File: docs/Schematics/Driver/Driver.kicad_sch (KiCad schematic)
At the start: 7 parts, among them J10 AUX_3V3, J11 AUX_GND, J9 AUX_5V

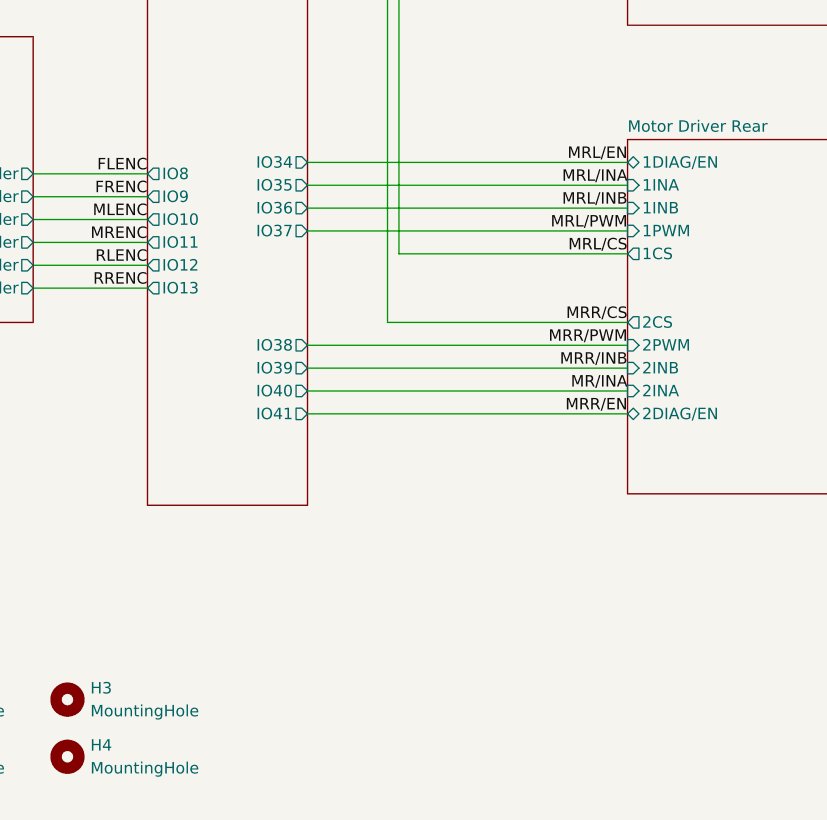
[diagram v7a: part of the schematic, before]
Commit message: First version of the routed board is done
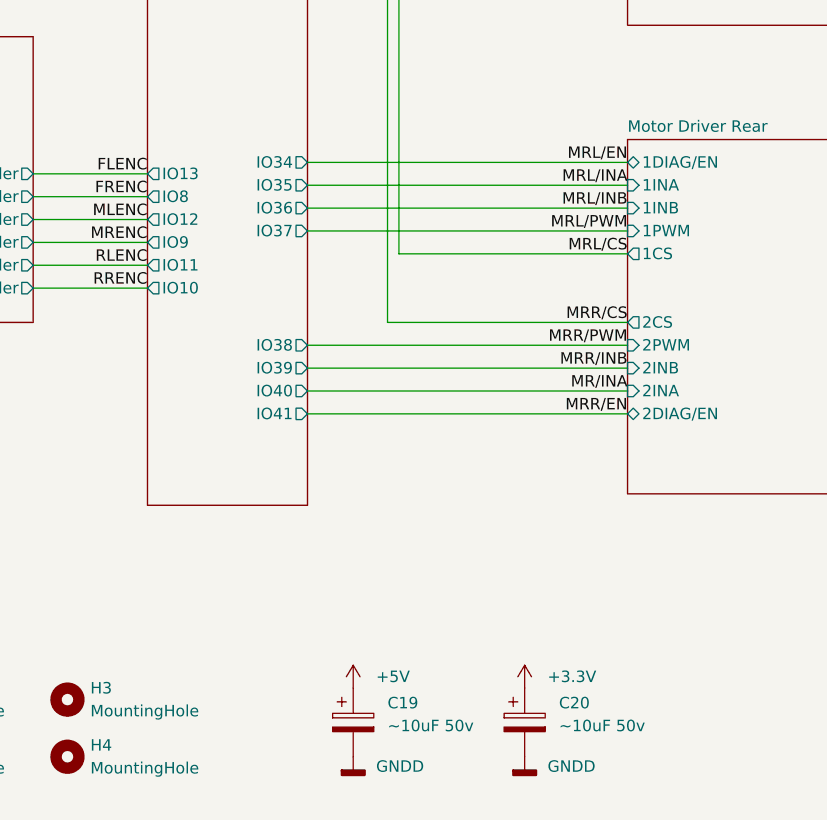
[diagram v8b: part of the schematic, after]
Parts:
- added C19, C20: ~10uF 50v, Capacitor_THT:CP_Radial_D8.0mm_P5.00mm, symbol Device:C_Polarized
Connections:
- net +3.3V: now also C20.1
- net +5V: now also C19.1
- net GNDD: now also C19.2, C20.2
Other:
- title: Arty Z7 IO expander card -> Arty Z7 IO Board
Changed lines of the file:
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@@
   (paper "A4")
   (title_block
-    (title "Arty Z7 IO expander card")
+    (title "Arty Z7 IO Board")
     (date "2022-12-24")
-    (rev "0.1")
+    (rev "${VER}")
     (company "HiQ")
   )
@@
     )
   )
+  (symbol (lib_id "power:GNDD") (at 127 190.5 0) (unit 1)
+    (in_bom yes) (on_board yes) (fields_autoplaced)
+    (property "Reference" "#PWR0103" (id 0) (at 127 196.85 0)
+      (effects (font (size 1.27 1.27)) hide)
+    )
+    (property "Value" "GNDD" (id 1) (at 129.54 191.5794 0)
+      (effects (font (size 1.27 1.27)) (justify left))
+    )
+    (property "Footprint" "" (id 2) (at 127 190.5 0)
+      (effects (font (size 1.27 1.27)) hide)
+    )
+    (property "Datasheet" "" (id 3) (at 127 190.5 0)
+      (effects (font (size 1.27 1.27)) hide)
+    )
+    (pin "1")
+  )
+  (symbol (lib_id "power:+5V") (at 127 182.88 0) (unit 1)
+    (in_bom yes) (on_board yes) (fields_autoplaced)
+    (property "Reference" "#PWR0105" (id 0) (at 127 186.69 0)
+      (effects (font (size 1.27 1.27)) hide)
+    )
+    (property "Value" "+5V" (id 1) (at 129.54 181.6099 0)
+      (effects (font (size 1.27 1.27)) (justify left))
+    )
+    (property "Footprint" "" (id 2) (at 127 182.88 0)
+      (effects (font (size 1.27 1.27)) hide)
+    )
+    (property "Datasheet" "" (id 3) (at 127 182.88 0)
+      (effects (font (size 1.27 1.27)) hide)
+    )
+    (pin "1")
+  )
+  (symbol (lib_id "power:GNDD") (at 146.05 190.5 0) (unit 1)
+    (in_bom yes) (on_board yes) (fields_autoplaced)
+    (property "Reference" "#PWR0104" (id 0) (at 146.05 196.85 0)
+      (effects (font (size 1.27 1.27)) hide)
+    )
+    (property "Value" "GNDD" (id 1) (at 148.59 191.5794 0)
+      (effects (font (size 1.27 1.27)) (justify left))
+    )
+    (property "Footprint" "" (id 2) (at 146.05 190.5 0)
+      (effects (font (size 1.27 1.27)) hide)
+    )
+    (property "Datasheet" "" (id 3) (at 146.05 190.5 0)
+      (effects (font (size 1.27 1.27)) hide)
+    )
+    (pin "1")
+  )
   (symbol (lib_id "Mechanical:MountingHole") (at 95.25 190.5 0) (unit 1)
     (in_bom yes) (on_board yes) (fields_autoplaced)
@@
     )
     (property "Datasheet" "" (id 3) (at 27.94 179.07 0)
+      (effects (font (size 1.27 1.27)) hide)
+    )
+    (pin "1")
+  )
+  (symbol (lib_id "Device:C_Polarized") (at 146.05 186.69 0) (unit 1)
+    (in_bom yes) (on_board yes) (fields_autoplaced)
+    (property "Reference" "C20" (id 0) (at 149.86 184.5309 0)
+      (effects (font (size 1.27 1.27)) (justify left))
+    )
+    (property "Value" "~10uF 50v" (id 1) (at 149.86 187.0709 0)
+      (effects (font (size 1.27 1.27)) (justify left))
+    )
+    (property "Footprint" "Capacitor_THT:CP_Radial_D8.0mm_P5.00mm" (id 2) (at 147.0152 190.5 0)
+      (effects (font (size 1.27 1.27)) hide)
+    )
+    (property "Datasheet" "~" (id 3) (at 146.05 186.69 0)
+      (effects (font (size 1.27 1.27)) hide)
+    )
+    (pin "1")
+    (pin "2")
+  )
+  (symbol (lib_id "Device:C_Polarized") (at 127 186.69 0) (unit 1)
+    (in_bom yes) (on_board yes) (fields_autoplaced)
+    (property "Reference" "C19" (id 0) (at 130.81 184.5309 0)
+      (effects (font (size 1.27 1.27)) (justify left))
+    )
+    (property "Value" "~10uF 50v" (id 1) (at 130.81 187.0709 0)
+      (effects (font (size 1.27 1.27)) (justify left))
+    )
+    (property "Footprint" "Capacitor_THT:CP_Radial_D8.0mm_P5.00mm" (id 2) (at 127.9652 190.5 0)
+      (effects (font (size 1.27 1.27)) hide)
+    )
+    (property "Datasheet" "~" (id 3) (at 127 186.69 0)
+      (effects (font (size 1.27 1.27)) hide)
+    )
+    (pin "1")
+    (pin "2")
+  )
+  (symbol (lib_id "power:+3.3V") (at 146.05 182.88 0) (unit 1)
+    (in_bom yes) (on_board yes) (fields_autoplaced)
+    (property "Reference" "#PWR0106" (id 0) (at 146.05 186.69 0)
+      (effects (font (size 1.27 1.27)) hide)
+    )
+    (property "Value" "+3.3V" (id 1) (at 148.59 181.6099 0)
+      (effects (font (size 1.27 1.27)) (justify left))
+    )
+    (property "Footprint" "" (id 2) (at 146.05 182.88 0)
+      (effects (font (size 1.27 1.27)) hide)
+    )
+    (property "Datasheet" "" (id 3) (at 146.05 182.88 0)
       (effects (font (size 1.27 1.27)) hide)
     )
@@
       (effects (font (size 1.27 1.27)) (justify right))
     )
-    (pin "IO11" output (at 104.14 133.35 180)
-      (effects (font (size 1.27 1.27)) (justify left))
-    )
-    (pin "IO12" output (at 104.14 135.89 180)
-      (effects (font (size 1.27 1.27)) (justify left))
-    )
-    (pin "IO13" output (at 104.14 138.43 180)
+    (pin "IO11" output (at 104.14 135.89 180)
+      (effects (font (size 1.27 1.27)) (justify left))
+    )
+    (pin "IO12" output (at 104.14 130.81 180)
+      (effects (font (size 1.27 1.27)) (justify left))
+    )
+    (pin "IO13" output (at 104.14 125.73 180)
       (effects (font (size 1.27 1.27)) (justify left))
     )
@@
       (effects (font (size 1.27 1.27)) (justify right))
     )
-    (pin "IO10" output (at 104.14 130.81 180)
-      (effects (font (size 1.27 1.27)) (justify left))
-    )
-    (pin "IO9" output (at 104.14 128.27 180)
+    (pin "IO10" output (at 104.14 138.43 180)
+      (effects (font (size 1.27 1.27)) (justify left))
+    )
+    (pin "IO9" output (at 104.14 133.35 180)
       (effects (font (size 1.27 1.27)) (justify left))
     )
@@
       (effects (font (size 1.27 1.27)) (justify right))
     )
-    (pin "IO8" output (at 104.14 125.73 180)
+    (pin "IO8" output (at 104.14 128.27 180)
       (effects (font (size 1.27 1.27)) (justify left))
     )
@@
       (reference "#PWR0102") (unit 1) (value "+5V") (footprint "")
     )
+    (path "/4e939897-1c6e-4519-843a-8d8f47b90389"
+      (reference "#PWR0103") (unit 1) (value "GNDD") (footprint "")
+    )
+    (path "/60bc5cbd-a9c4-4c0c-81e7-fb3a28f22eea"
+      (reference "#PWR0104") (unit 1) (value "GNDD") (footprint "")
+    )
+    (path "/548a5c90-6269-42f2-a03d-852079803222"
+      (reference "#PWR0105") (unit 1) (value "+5V") (footprint "")
+    )
+    (path "/917950b5-a07b-4005-91b7-d1dbcacbda89"
+      (reference "#PWR0106") (unit 1) (value "+3.3V") (footprint "")
+    )
     (path "/beaab9be-ccdc-4b38-ab36-75ff11f07b55/b4056e8e-2685-4bce-b62b-c0b98923e0d3/136397f4-377d-4025-90d0-0706659409fa"
       (reference "C1") (unit 1) (value "C_Polarized") (footprint "Capacitor_SMD:C_0805_2012Metric_Pad1.18x1.45mm_HandSolder")
@@
       (reference "C18") (unit 1) (value "C_Polarized") (footprint "Capacitor_SMD:C_0805_2012Metric_Pad1.18x1.45mm_HandSolder")
     )
+    (path "/7bb11ea5-ff55-4e06-8a8b-f5c5ce07742b"
+      (reference "C19") (unit 1) (value "~10uF 50v") (footprint "Capacitor_THT:CP_Radial_D8.0mm_P5.00mm")
+    )
+    (path "/7405d021-0a38-4108-a4e6-e06be8d12996"
+      (reference "C20") (unit 1) (value "~10uF 50v") (footprint "Capacitor_THT:CP_Radial_D8.0mm_P5.00mm")
+    )
     (path "/963b2533-799e-4061-9fee-caedf26cfde0"
